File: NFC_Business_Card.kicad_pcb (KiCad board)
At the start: 2 copper layers, 85.6 x 54 mm, 0 parts

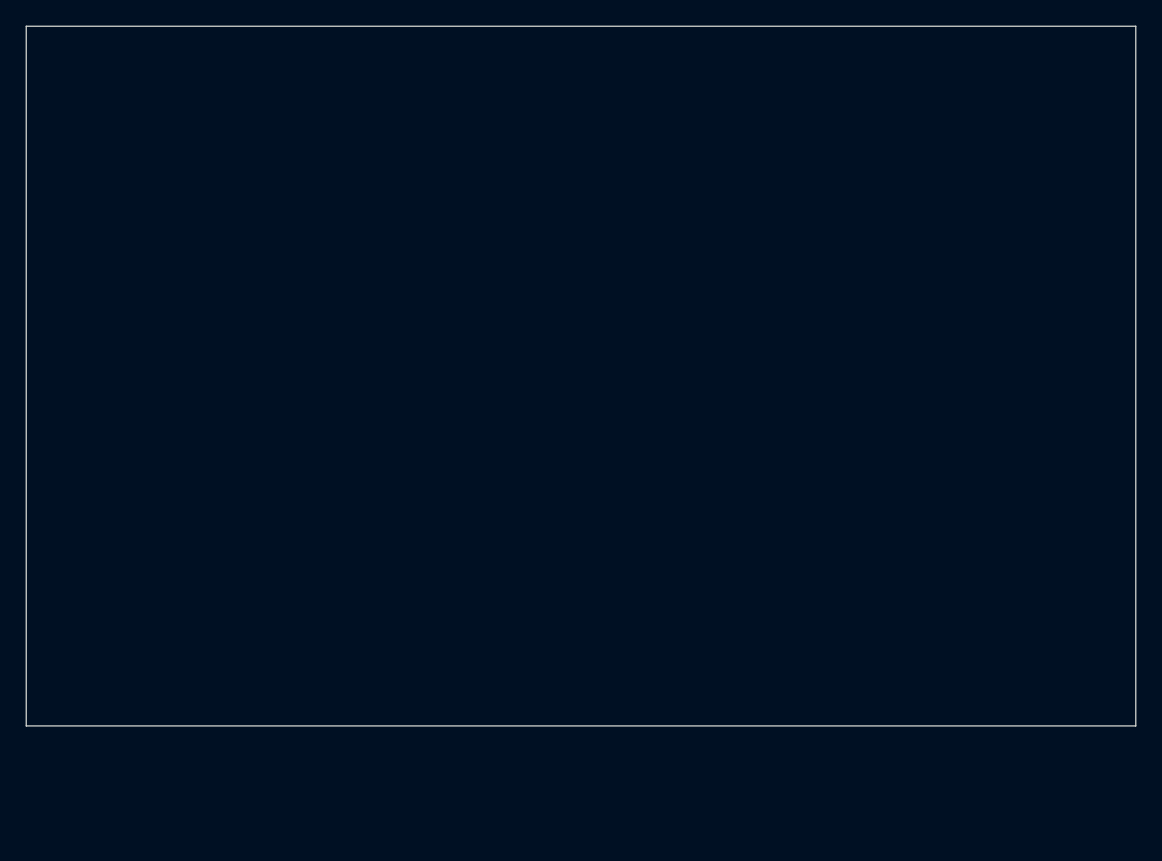
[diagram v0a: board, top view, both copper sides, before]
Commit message: Added antenna to PCB
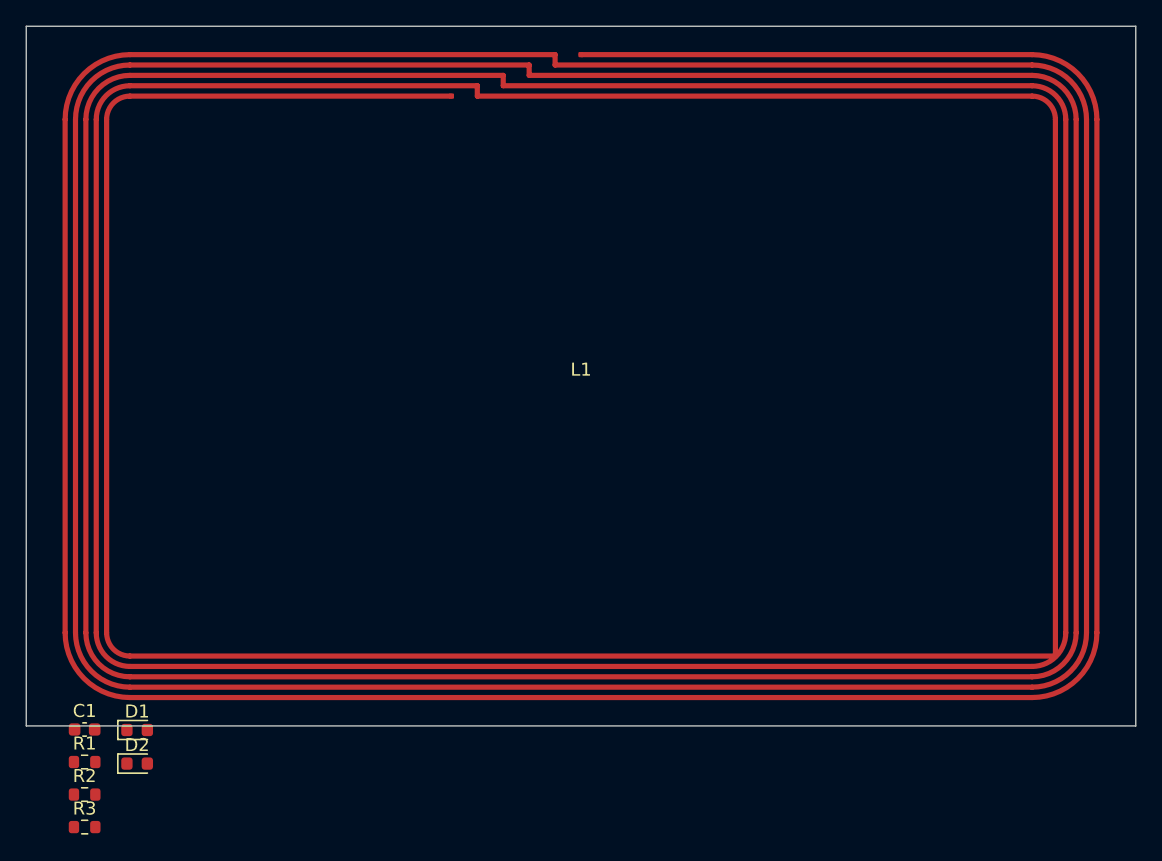
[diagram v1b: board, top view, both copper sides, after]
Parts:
- added C1: 10nF, Capacitor_SMD:C_0603_1608Metric, F.Cu at (54.5, 104.3)
- added D1: RED LED, LED_SMD:LED_0603_1608Metric, F.Cu at (58.6, 104.3)
- added D2: RED LED, LED_SMD:LED_0603_1608Metric, F.Cu at (58.6, 106.9)
- added L1: PCB Antenna ~4.68uH, NFC_Custom:NFC_80x50_5T, F.Cu at (92.8, 77.0)
- added R1: 1k, Resistor_SMD:R_0603_1608Metric, F.Cu at (54.5, 106.8)
- added R2: 1k, Resistor_SMD:R_0603_1608Metric, F.Cu at (54.5, 109.3)
- added R3: 0R, Resistor_SMD:R_0603_1608Metric, F.Cu at (54.5, 111.8)

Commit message: Placed most components
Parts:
- added G***: Ryan_Robot_Outline_29mm, NFC_Custom:Ryan_Robot_Outline_29mm, F.Cu at (115.0, 77.0)
- moved R3 77.7 mm to (124.0, 77.0), turned to -90 degrees
- moved D2 71.4 mm to (118.4, 67.9)
- moved R2 71.3 mm to (116.5, 74.0), turned to 180 degrees
- moved R1 67.5 mm to (113.5, 74.0)
- moved D1 64.3 mm to (111.6, 67.9)
- moved C1 58.3 mm to (106.0, 77.0), turned to -90 degrees

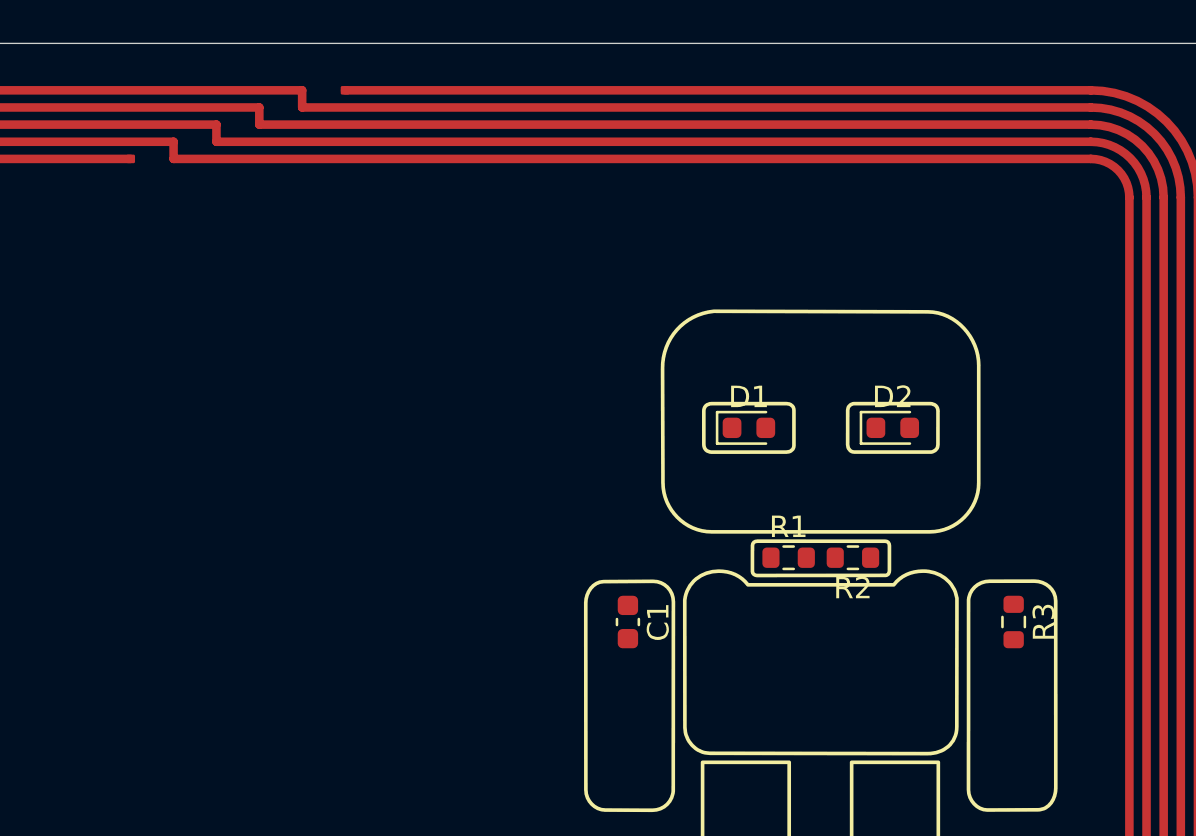
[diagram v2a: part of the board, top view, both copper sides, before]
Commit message: Added base routing
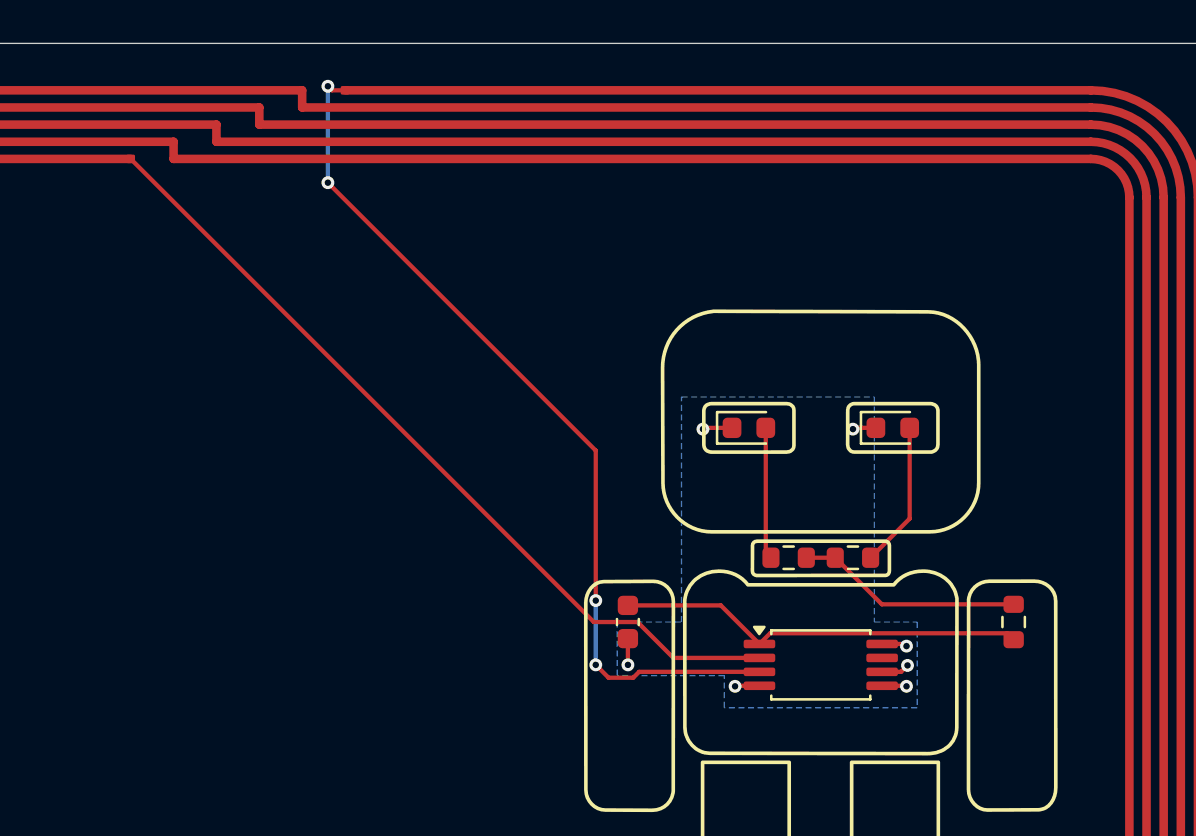
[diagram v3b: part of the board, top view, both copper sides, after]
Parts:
- added U1: ST25DV04KC-IE6T3, Package_SO:TSSOP-8_4.4x3mm_P0.65mm, F.Cu at (115.0, 79.0)
- turned C1 to 90 degrees
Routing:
- net Net-(U1-AC1): track 0.00 -> 41.1 mm, vias 0 -> 4
- net Net-(U1-AC0): track 0.00 -> 39.0 mm
- net /V_EH: track 0.00 -> 19.1 mm
- net Net-(R1-Pad2): track 0.00 -> 10.6 mm
- net GND: track 0.00 -> 8.49 mm, vias 0 -> 7
- net Net-(D2-A): track 0.00 -> 6.82 mm
- net Net-(D1-A): track 0.00 -> 6.16 mm
- added copper zone on B.Cu, net GND

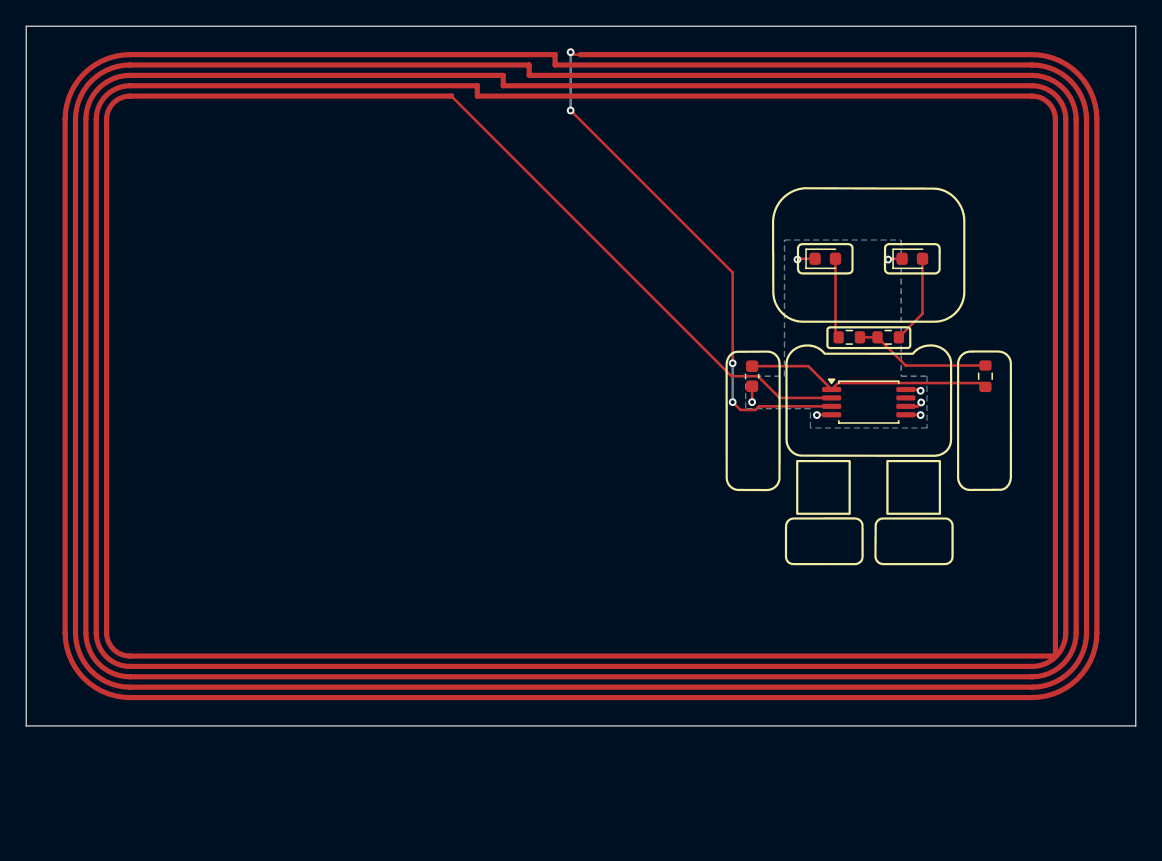
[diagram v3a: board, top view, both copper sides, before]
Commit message: Adjusted AC0 and Ac1 for safer
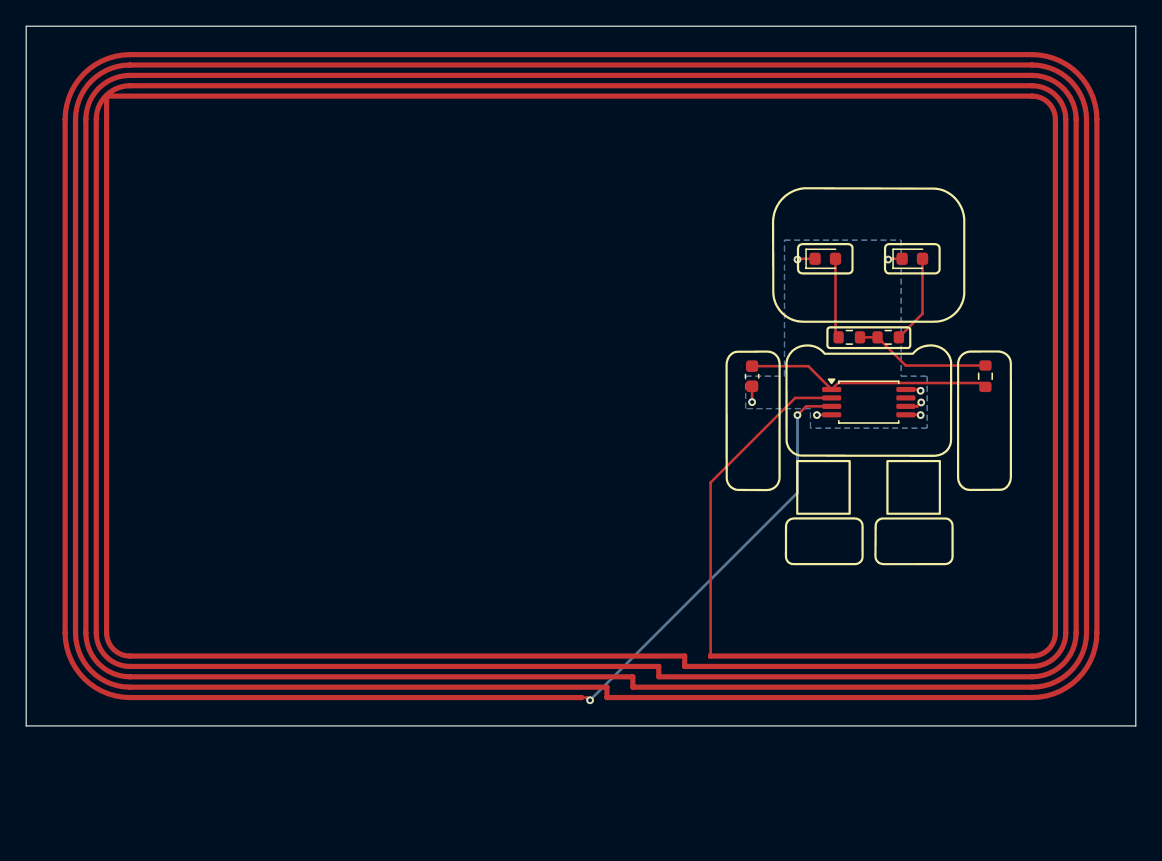
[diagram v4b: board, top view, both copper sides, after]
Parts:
- turned L1 to 180 degrees
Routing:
- net Net-(U1-AC0): track 39.0 -> 25.4 mm
- net Net-(U1-AC1): track 41.1 -> 32.3 mm, vias 4 -> 2

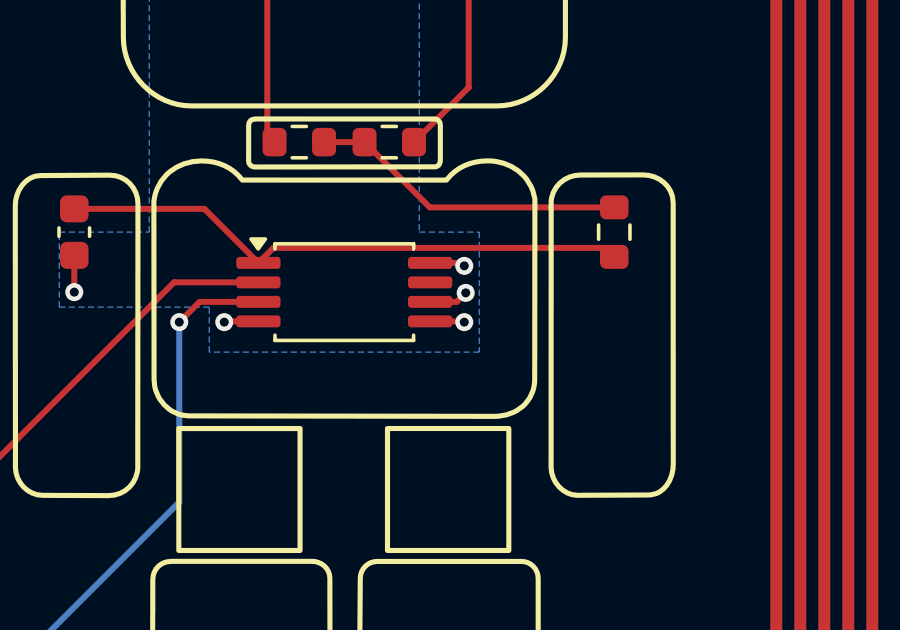
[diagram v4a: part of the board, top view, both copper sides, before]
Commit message: Fixed DRC and ERC errors
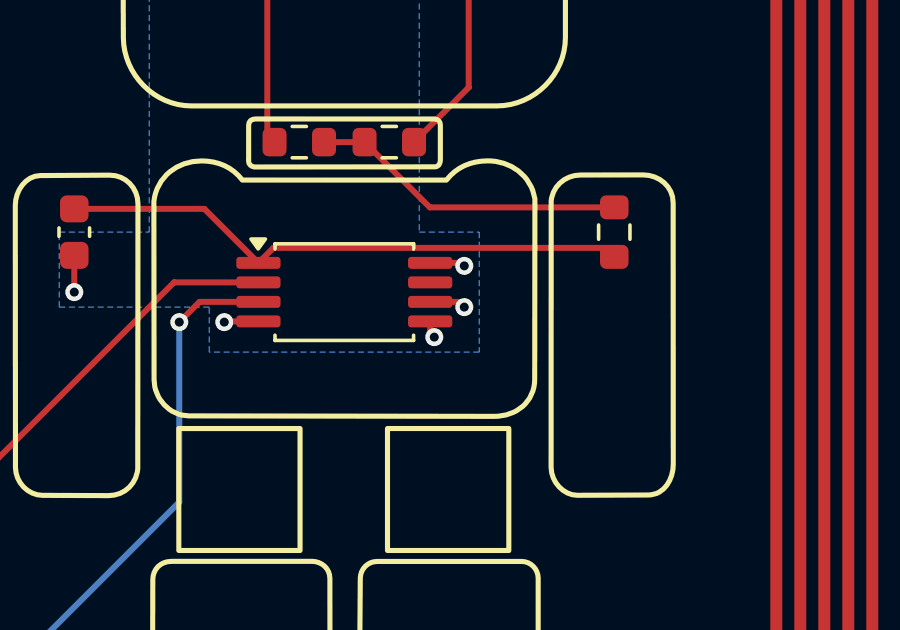
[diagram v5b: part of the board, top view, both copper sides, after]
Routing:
- net GND: track 8.49 -> 7.82 mm
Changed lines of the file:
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@@
-	)
-	(segment
-		(start 118.74752 79.325)
-		(end 119.047492 79.025028)
-		(width 0.2)
-		(layer "F.Cu")
-		(net "GND")
 	)
 	(segment
@@
 	)
 	(segment
-		(start 118.975 79.975)
-		(end 119 80)
-		(width 0.2)
-		(layer "F.Cu")
-		(net "GND")
-	)
-	(segment
-		(start 117.8625 79.975)
-		(end 118.975 79.975)
+		(start 117.8625 80.3625)
+		(end 118 80.5)
 		(width 0.2)
 		(layer "F.Cu")
@@
 	(segment
 		(start 117.8625 79.325)
-		(end 118.74752 79.325)
+		(end 118.825 79.325)
+		(width 0.2)
+		(layer "F.Cu")
+		(net "GND")
+	)
+	(segment
+		(start 119 79.5)
+		(end 118.825 79.325)
+		(width 0.2)
+		(layer "F.Cu")
+		(net "GND")
+	)
+	(segment
+		(start 117.8625 79.975)
+		(end 117.8625 80.3625)
 		(width 0.2)
 		(layer "F.Cu")
@@
 	)
 	(via
-		(at 119.047492 79.025028)
-		(size 0.6)
-		(drill 0.3)
-		(layers "F.Cu" "B.Cu")
-		(net "GND")
-	)
-	(via
-		(at 119 80)
+		(at 118 80.5)
 		(size 0.6)
 		(drill 0.3)
@@
 		(size 0.6)
 		(drill 0.3)
+		(layers "F.Cu" "B.Cu")
+		(net "GND")
+	)
+	(via
+		(at 119 79.5)
+		(size 0.6)
+		(drill 0.3)

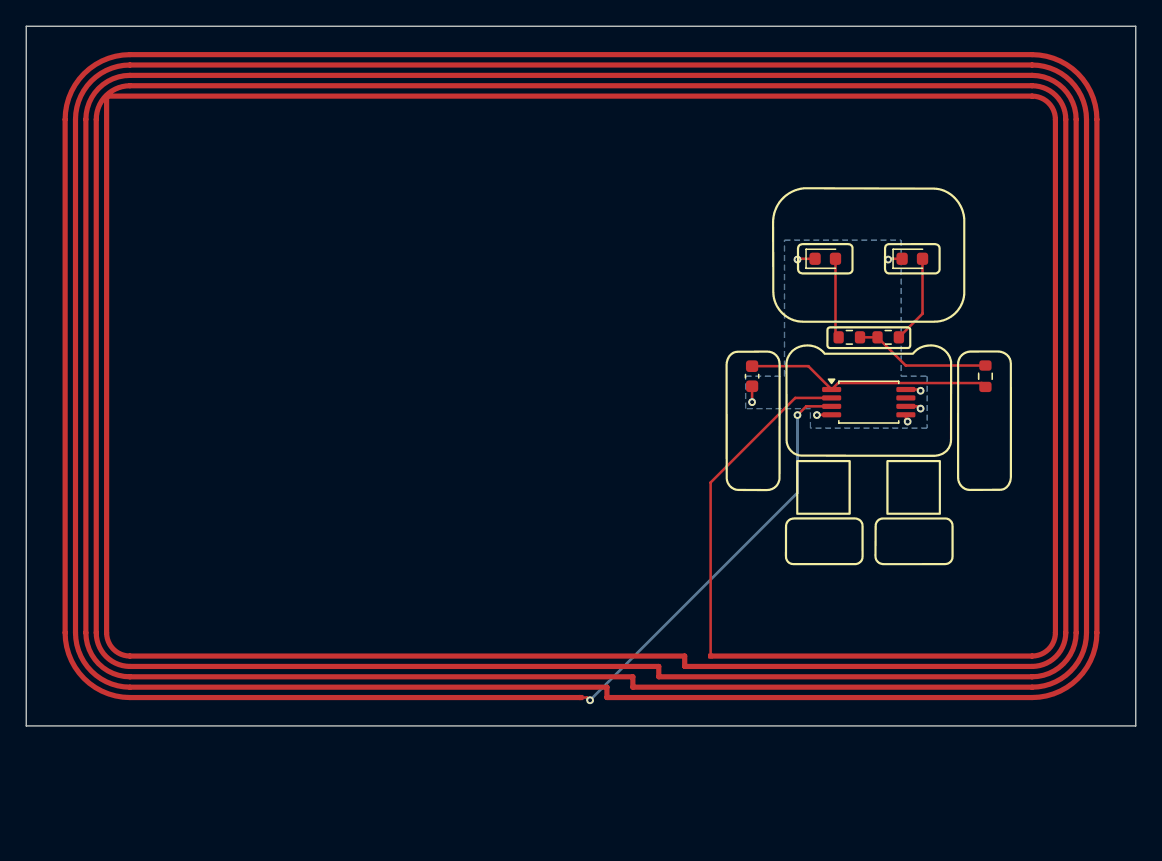
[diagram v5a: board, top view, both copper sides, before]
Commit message: Added front silkscreen
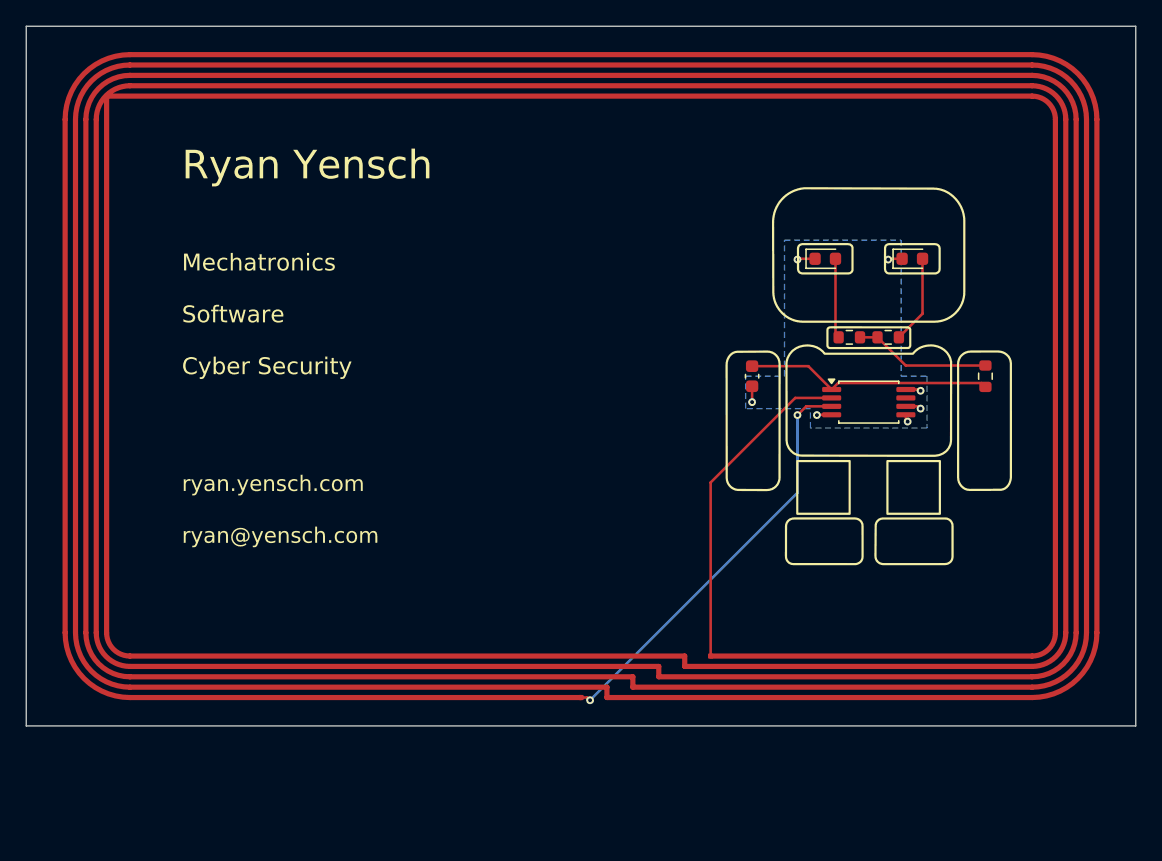
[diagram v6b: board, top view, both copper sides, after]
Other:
- board text added: "Cyber Security"
- board text added: "Mechatronics"
- board text added: "Ryan Yensch"
- board text added: "Software"
- board text added: "ryan.yensch.com"
- board text added: "ryan@yensch.com"
